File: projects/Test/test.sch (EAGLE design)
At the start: 47 parts, among them J2 1755529, U1 STM32F405RGT6, U2 CSD88584Q5DCT, U3 CSD88584Q5DCT, U4 CSD88584Q5DCT, Y1 ECS-80-S-4X

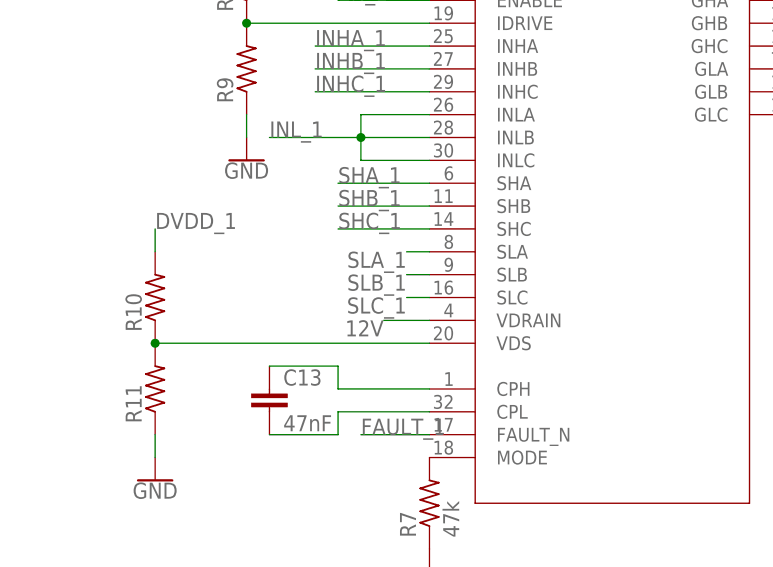
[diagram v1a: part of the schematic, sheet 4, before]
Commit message: Finished test board (before ratsnest)
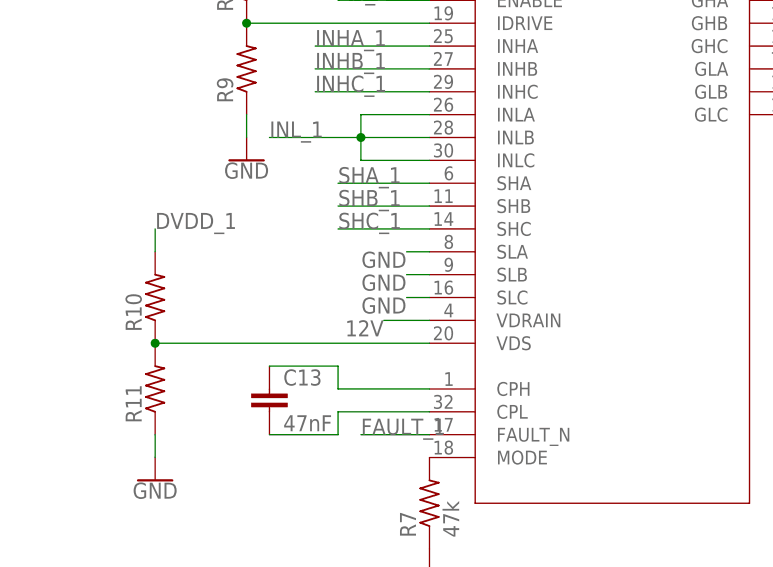
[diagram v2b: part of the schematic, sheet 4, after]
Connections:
- removed net SLA_1: U$2G$1.SLA, U3.PGND, U3.PGND_2, U3.PGND_3, U3.PGND_4, U3.PGND_5, U3.PGND_6, U3.PGND_7, U3.PGND_8, U3.PGND_9
- removed net SLB_1: U$2G$1.SLB, U4.PGND, U4.PGND_2, U4.PGND_3, U4.PGND_4, U4.PGND_5, U4.PGND_6, U4.PGND_7, U4.PGND_8, U4.PGND_9
- removed net SLC_1: U$2G$1.SLC, U2.PGND, U2.PGND_2, U2.PGND_3, U2.PGND_4, U2.PGND_5, U2.PGND_6, U2.PGND_7, U2.PGND_8, U2.PGND_9
- net GND: now also U$2G$1.SLA, U$2G$1.SLB, U$2G$1.SLC, U2.PGND, U2.PGND_2, U2.PGND_3, U2.PGND_4, U2.PGND_5, U2.PGND_6, U2.PGND_7, U2.PGND_8, U2.PGND_9, U3.PGND, U3.PGND_2, U3.PGND_3, U3.PGND_4, U3.PGND_5, U3.PGND_6, U3.PGND_7, U3.PGND_8, U3.PGND_9, U4.PGND, U4.PGND_2, U4.PGND_3, U4.PGND_4, U4.PGND_5, U4.PGND_6, U4.PGND_7, U4.PGND_8, U4.PGND_9
